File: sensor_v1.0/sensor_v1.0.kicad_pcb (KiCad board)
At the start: 2 copper layers, 49.8 x 49.8 mm, 4 parts

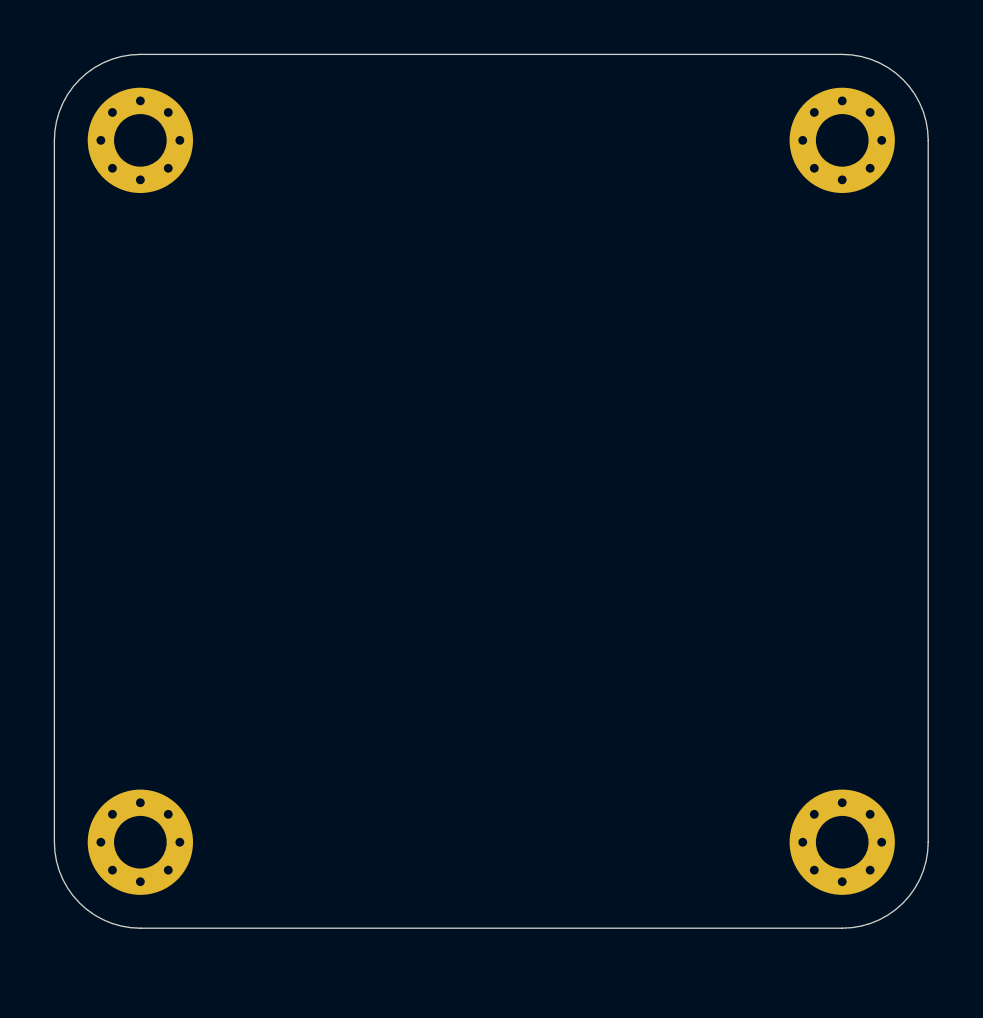
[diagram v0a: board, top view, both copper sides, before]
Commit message: sensor board v1.0 mostly routed
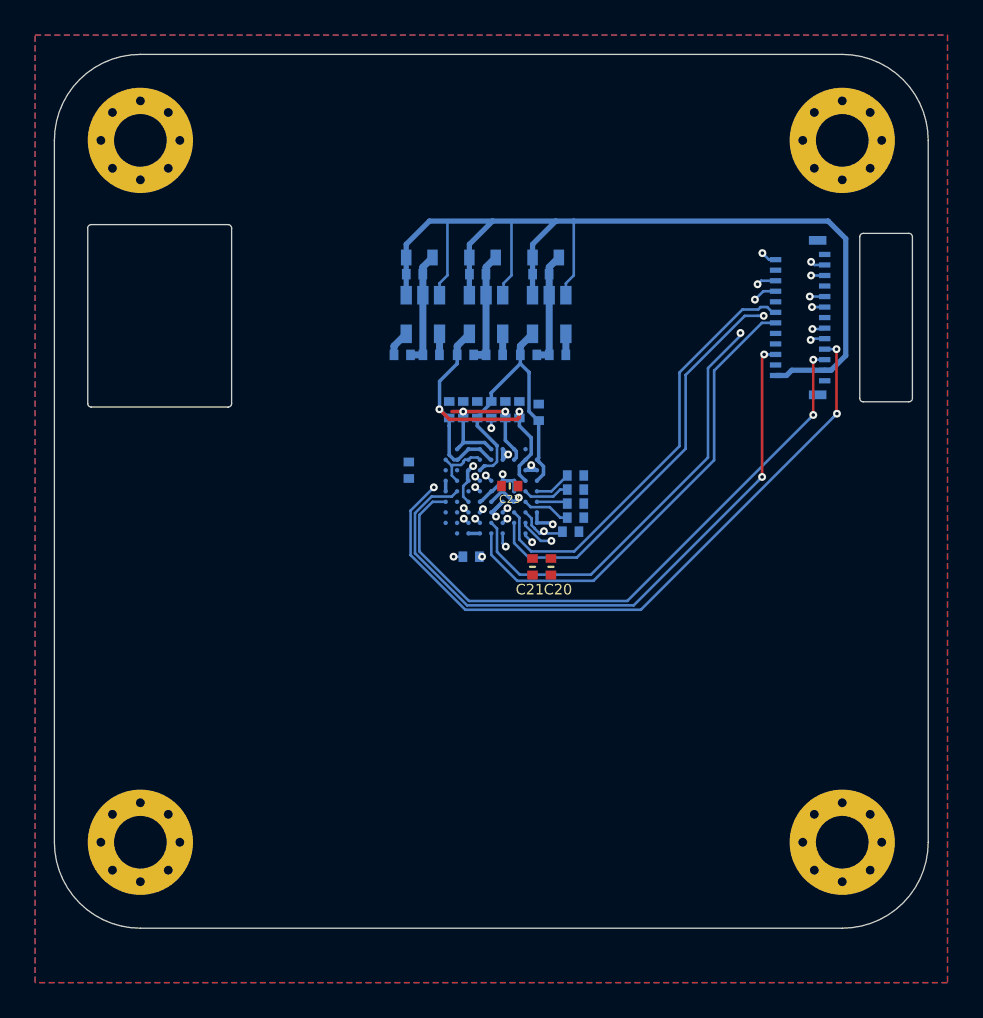
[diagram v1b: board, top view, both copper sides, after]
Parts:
- added C1: 10u, otter:C_0603, B.Cu at (70.9, 61.7)
- added C10: 100n, otter:C_0402, B.Cu at (77.1, 67.2)
- added C11: 100n, otter:C_0402, B.Cu at (69.9, 67.2)
- added C12: 100n, otter:C_0402, B.Cu at (73.5, 67.2)
- added C14: 100n, otter:C_0402, B.Cu at (73.4, 70.3)
- added C15: 100n, otter:C_0402, B.Cu at (70.3, 73.8)
- added C16: 100n, otter:C_0402, B.Cu at (74.2, 70.3)
- added C17: 100n, otter:C_0402, B.Cu at (75.8, 70.3)
- added C18: 100n, otter:C_0402, B.Cu at (72.6, 70.3)
- added C19: 100n, otter:C_0402, B.Cu at (79.5, 77.3)
- added C2: 10u, otter:C_0603, B.Cu at (74.5, 61.7)
- added C20: 100n, otter:C_0402, F.Cu at (78.4, 79.3)
- added C21: 100n, otter:C_0402, F.Cu at (77.3, 79.3)
- added C22: 100n, otter:C_0402, B.Cu at (77.7, 70.5)
- added C23: 100n, otter:C_0402, F.Cu at (76.0, 74.7)
- added C24: 100n, otter:C_0402, B.Cu at (76.6, 70.3)
- added C25: 1u, otter:C_0402, B.Cu at (79.8, 74.1)
- added C26: 1u, otter:C_0402, B.Cu at (79.8, 74.9)
- added C27: 1u, otter:C_0402, B.Cu at (79.8, 75.7)
- added C28: 1u, otter:C_0402, B.Cu at (79.8, 76.5)
- added C3: 10u, otter:C_0603, B.Cu at (78.1, 61.7)
- added C4: 100n, otter:C_0402, B.Cu at (70.6, 62.6)
- added C5: 100n, otter:C_0402, B.Cu at (74.2, 62.6)
- added C6: 100n, otter:C_0402, B.Cu at (77.8, 62.6)
- added C7: 10n, otter:C_0402, B.Cu at (78.8, 67.2)
- added C8: 10n, otter:C_0402, B.Cu at (71.6, 67.2)
- added C9: 10n, otter:C_0402, B.Cu at (75.2, 67.2)
- added J1: FH35C-25S, otter:FH35C-25S, B.Cu at (93.7, 65.1)
- added R1: 10k, otter:R_0402, B.Cu at (75.0, 70.3)
- added R2: 22, otter:R_0402, B.Cu at (73.8, 78.7)
- added U1: LP2985-2.8, Package_TO_SOT_SMD:SOT-23-5, B.Cu at (78.3, 64.9)
- added U2: LP2985-1.8, Package_TO_SOT_SMD:SOT-23-5, B.Cu at (71.1, 64.9)
- added U3: LP2985-1.2, Package_TO_SOT_SMD:SOT-23-5, B.Cu at (74.7, 64.9)
- added U4: OS05A10-SMU, otter:OS05A10, B.Cu at (75.0, 75.0)
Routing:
- net +3V3: track 0.00 -> 62.8 mm
- net MIPI_RESET: track 0.00 -> 42.0 mm, vias 0 -> 4
- net MIPI_SDA: track 0.00 -> 36.9 mm, vias 0 -> 2
- net MIPI_SCK: track 0.00 -> 35.7 mm, vias 0 -> 2
- net GND: track 0.00 -> 34.0 mm, vias 0 -> 5
- net MIPI_D3_P: track 0.00 -> 33.5 mm, vias 0 -> 2
- net MIPI_CLK_P: track 0.00 -> 29.9 mm, vias 0 -> 2
- net MIPI_D3_N: track 0.00 -> 29.6 mm, vias 0 -> 2
- net MIPI_D2_N: track 0.00 -> 28.4 mm, vias 0 -> 2
- net MIPI_D0_N: track 0.00 -> 27.6 mm, vias 0 -> 2
- net MIPI_CLK_N: track 0.00 -> 27.1 mm
- net MIPI_D1_P: track 0.00 -> 26.1 mm, vias 0 -> 2
- net Net-(J1-Pad17): track 0.00 -> 25.3 mm, vias 0 -> 2
- net +2V8: track 0.00 -> 25.1 mm, vias 0 -> 2
- net MIPI_D0_P: track 0.00 -> 24.9 mm
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- added copper zone on B.Cu, net GND
- added copper zone on F.Cu, net GND
- added copper zone on In1.Cu, net GND
- added copper zone on In2.Cu, net GND
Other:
- outline, holes or cut-outs redrawn
- copper layers 2 -> 4
- net class Default: clearance 0.2 -> 0.1; trace_width 0.25 -> 0.2
- rule pad_to_mask_clearance: 0.051 -> 0
- rule trace_clearance: 0.2 -> 0.1
- rule trace_min: 0.2 -> 0.15
- rule via_min_drill: 0.3 -> 0.2

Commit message: routing 100%
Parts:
- added C29: 100n, otter:C_0402, B.Cu at (74.3, 79.7)
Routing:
- net +1V2: track 24.8 -> 46.2 mm, vias 4 -> 5
- net +1V8: track 16.1 -> 33.9 mm, vias 4 -> 6
- net GND: track 34.0 -> 45.0 mm, vias 5 -> 16
- net +2V8: track 25.1 -> 31.0 mm, vias 2 -> 3
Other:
- board text added: "TODO Diffpair length maching Diffpair length matching with regard to otter board credentials + version number gnd vias"

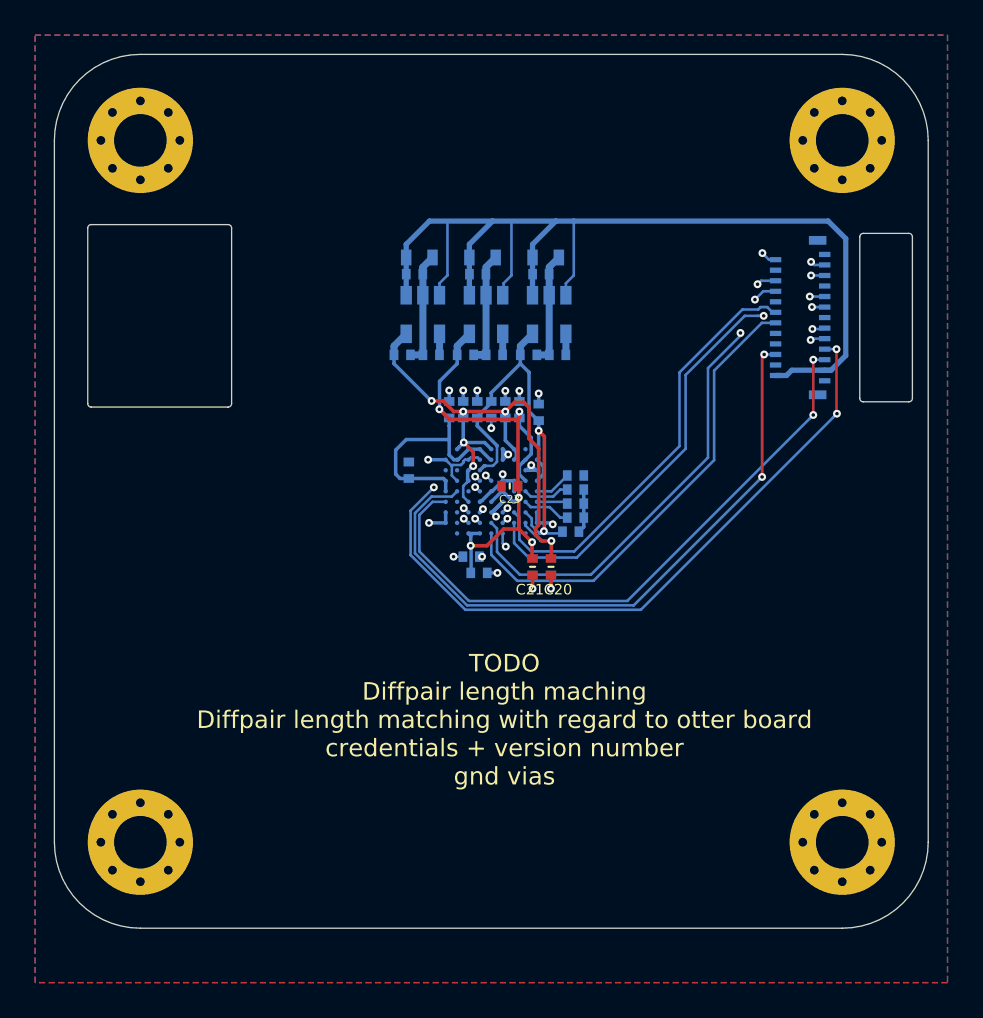
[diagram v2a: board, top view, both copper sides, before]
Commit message: fixed MIPI pinout, added pullups, fixed silkscreen
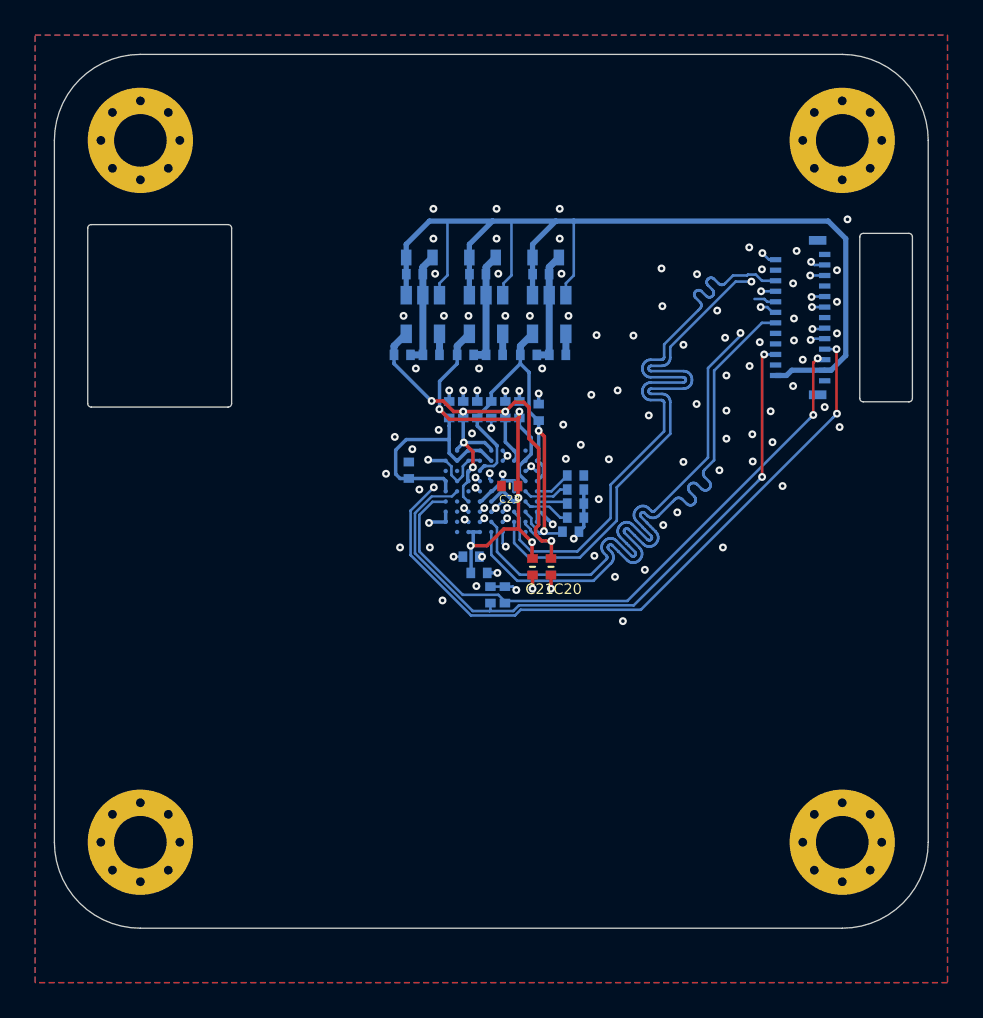
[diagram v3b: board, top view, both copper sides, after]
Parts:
- added R3: 10k, otter:R_0402, B.Cu at (75.8, 80.9)
- added R4: 10k, otter:R_0402, B.Cu at (75.0, 80.9)
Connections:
- U4 pad G3: MIPI_D0_P -> MIPI_D2_P
- U4 pad G4: MIPI_D1_P -> MIPI_D0_P
- U4 pad G6: MIPI_D2_P -> MIPI_D1_P
- U4 pad H3: MIPI_D0_N -> MIPI_D2_N
- U4 pad H4: MIPI_D1_N -> MIPI_D0_N
- U4 pad H6: MIPI_D2_N -> MIPI_D1_N
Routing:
- net MIPI_D1_N: track 23.4 -> 37.3 mm
- net MIPI_D0_P: track 24.9 -> 38.0 mm, vias 0 -> 2
- net MIPI_D2_P: track 24.4 -> 36.2 mm, vias 2 -> 0
- net MIPI_D1_P: track 26.1 -> 37.3 mm
- net MIPI_D0_N: track 27.6 -> 38.1 mm
- net MIPI_CLK_N: track 27.1 -> 37.2 mm
- net MIPI_D2_N: track 28.4 -> 36.2 mm
- net MIPI_CLK_P: track 29.9 -> 37.2 mm
- net +2V8: track 31.0 -> 34.9 mm, vias 3 -> 4
- net MIPI_D3_N: track 29.6 -> 33.2 mm
- net Net-(J1-Pad17): track 25.3 -> 27.0 mm
- net GND: track 45.0 -> 43.5 mm, vias 16 -> 95
- net MIPI_SDA: track 36.9 -> 37.7 mm
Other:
- rule trace_min: 0.15 -> 0.1127
- board text added: "OtterCam-s3 OS05A10/20 Board Jana Marie Hemsing @JanHenrikH 2021 rev 1.1 github.com/Jana-Marie/OtterCam-s3"
- board text removed: "TODO Diffpair length maching Diffpair length matching with regard to otter board credentials + version number gnd vias"
